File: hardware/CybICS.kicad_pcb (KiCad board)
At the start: 2 copper layers, 160 x 100 mm, 66 parts, among them J1 Raspberry_Pi_2_3, J2 Conn_01x03_Pin, J3 Conn_01x05_Pin, SW1 SW_Push, SW2 SW_Push, U1 STM32G070RBTx

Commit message: Updated hardware
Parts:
- added R29: 10kR, Resistor_SMD:R_0805_2012Metric_Pad1.20x1.40mm_HandSolder, F.Cu at (98.0, 133.0)
- added R30: 10kR, Resistor_SMD:R_0805_2012Metric_Pad1.20x1.40mm_HandSolder, F.Cu at (102.0, 133.0)
- added R31: 10kR, Resistor_SMD:R_0805_2012Metric_Pad1.20x1.40mm_HandSolder, F.Cu at (106.0, 133.0)
- added R32: 10kR, Resistor_SMD:R_0805_2012Metric_Pad1.20x1.40mm_HandSolder, F.Cu at (110.0, 133.0)
- added R33: 10kR, Resistor_SMD:R_0805_2012Metric_Pad1.20x1.40mm_HandSolder, F.Cu at (114.0, 133.0)
- added R34: 10kR, Resistor_SMD:R_0805_2012Metric_Pad1.20x1.40mm_HandSolder, F.Cu at (118.0, 133.0)
- added R35: 10kR, Resistor_SMD:R_0805_2012Metric_Pad1.20x1.40mm_HandSolder, F.Cu at (122.0, 133.0)
- added R36: 10kR, Resistor_SMD:R_0805_2012Metric_Pad1.20x1.40mm_HandSolder, F.Cu at (198.0, 112.0)
- added R37: 1kR, Resistor_SMD:R_0805_2012Metric_Pad1.20x1.40mm_HandSolder, F.Cu at (202.0, 112.0)
- added SW3: SW_Push, Button_Switch_THT:SW_PUSH_6mm_H5mm, F.Cu at (199.8, 102.8)
- moved RV1 23.9 mm to (124.0, 117.7), turned to 90 degrees
- moved R25 4.58 mm to (117.8, 107.0)
- moved SW1 3.80 mm to (54.5, 109.8)
- moved D13 3.20 mm to (55.3, 139.0)
- moved R20 3.20 mm to (59.8, 139.0)
- moved R26 3.08 mm to (117.8, 104.5)
- moved R21 2.92 mm to (117.8, 94.5)
- moved D11 2.80 mm to (55.3, 123.0)
- moved R11 2.80 mm to (59.8, 123.0)
- moved R23 1.58 mm to (117.8, 102.0)
- moved R22 1.42 mm to (117.8, 97.0)
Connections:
- U1 pad 36: unconnected-(U1-PA8-Pad36) -> /PA8
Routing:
- net /PA8: track 0.00 -> 120.7 mm, vias 0 -> 1
- net GND: track 16.4 -> 32.4 mm, vias 8 -> 16
- net Net-(DS1-VO): track 9.17 -> 21.9 mm, vias 0 -> 2
- net Net-(R37-Pad2): track 0.00 -> 11.2 mm
- net /PA3: track 21.8 -> 32.2 mm
- net /PA6: track 30.2 -> 40.4 mm
- net /PA4: track 26.3 -> 36.4 mm
- net /PA2: track 17.3 -> 27.2 mm
- net /PA1: track 16.5 -> 26.2 mm
- net /PA0: track 15.6 -> 25.2 mm
- net /PA5: track 28.3 -> 37.8 mm
- net /STMnrst: track 70.0 -> 66.2 mm
- net /ST_heartbeat: track 36.9 -> 34.1 mm
- net Net-(D18-K): track 66.6 -> 64.7 mm
- net /PA12: track 19.0 -> 17.2 mm
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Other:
- board text added: "3.3V Good"
- board text added: "Contrast"
- board text added: "Display"
- board text added: "GND"
- board text added: "MCU reset"
- board text added: "RPi Heartbeat"
- board text added: "Raspberry Pi"
- board text added: "STM Heartbeat"

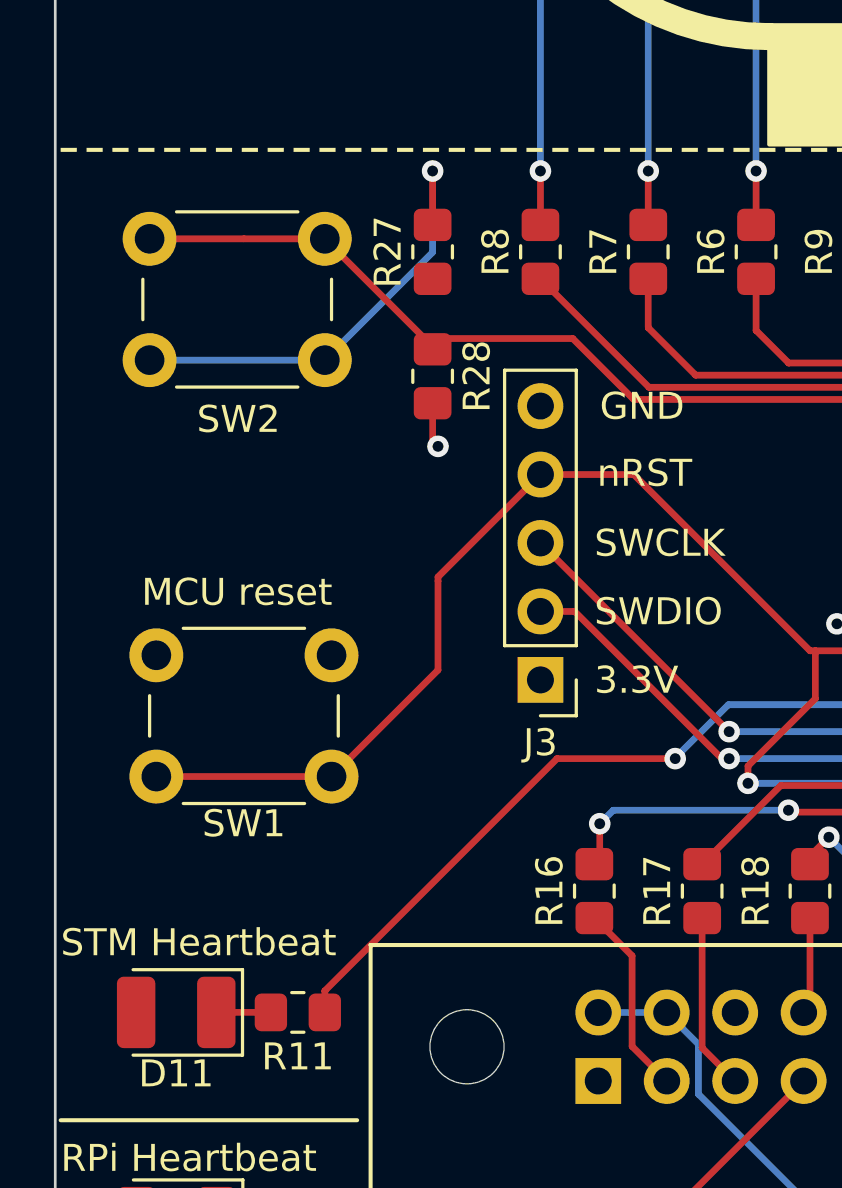
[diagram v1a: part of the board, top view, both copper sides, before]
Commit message: This commit will: - fix #2 - Added usb-c (only for power supply) - Added first attack example
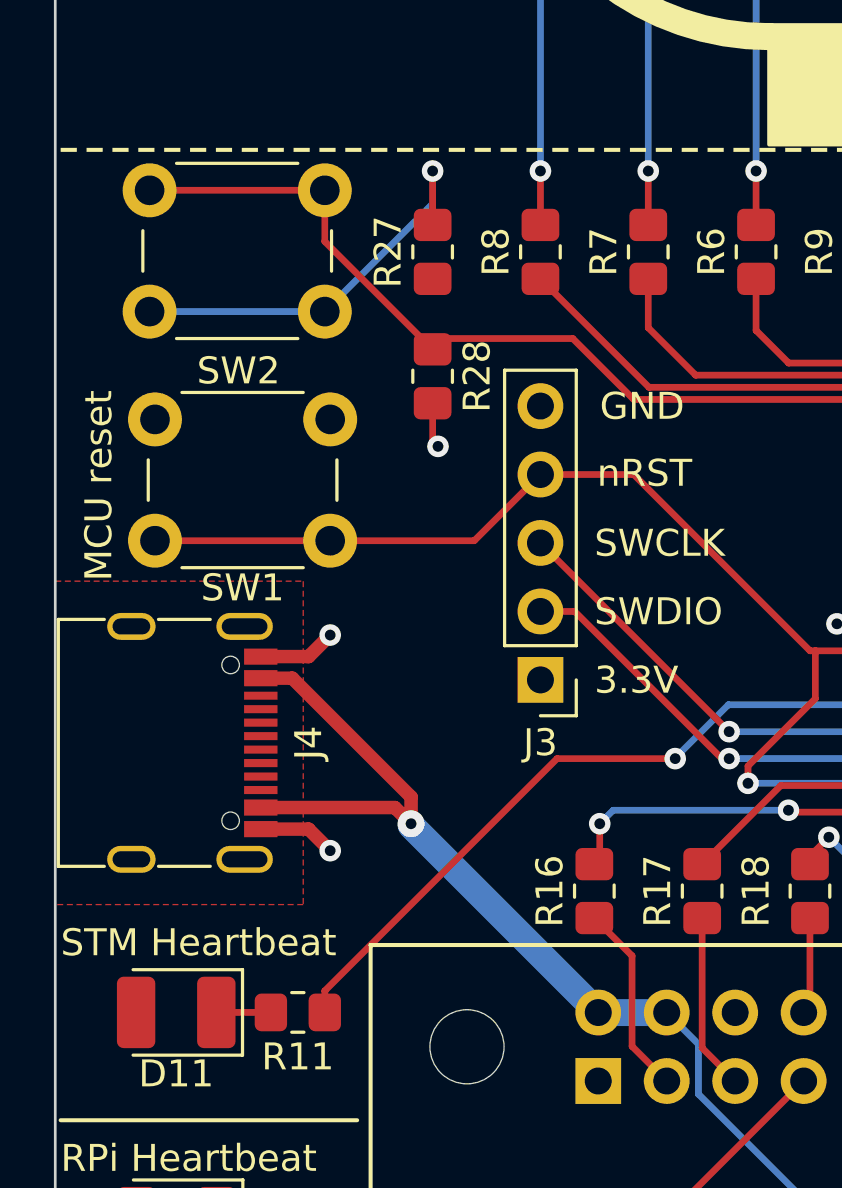
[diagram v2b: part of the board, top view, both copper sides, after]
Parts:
- added J4: USB_C_Receptacle_USB2.0, Connector_USB:USB_C_Receptacle_G-Switch_GT-USB-7010ASV, F.Cu at (54.7, 113.0)
- moved SW1 8.75 mm to (54.5, 101.0)
- moved SW2 1.80 mm to (54.3, 92.5)
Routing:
- net +5V: track 79.6 -> 103.1 mm, vias 0 -> 1
- net /STMnrst: track 66.2 -> 60.6 mm
- net GND: track 32.4 -> 37.6 mm, vias 16 -> 18
- net /PC10: track 39.5 -> 41.8 mm
- net Net-(R27-Pad2): track 17.2 -> 15.4 mm
- added copper zone on F.Cu, net Earth_Protective
